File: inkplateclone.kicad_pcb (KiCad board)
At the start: 2 copper layers, 73 parts, among them J1 ED060SC7, J2 USB_C_Receptacle_USB2.0, Q1 Q_NMOS_GSD, Q2 Q_NMOS_GSD, Q3 Q_PMOS_GSD, U1 TPS65186, U2 ED097OC1, U3 MCP23017_SO, U4 ESP32-WROVER, U5 CH340C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

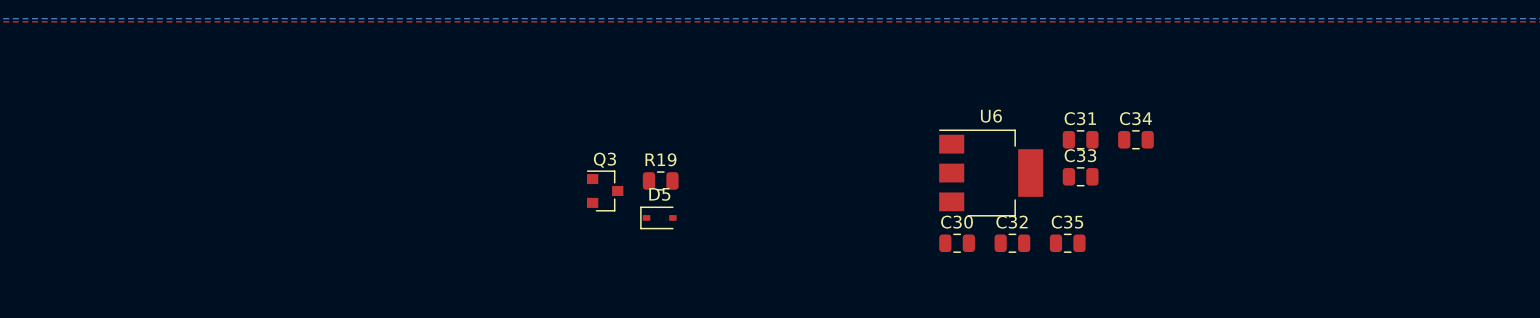
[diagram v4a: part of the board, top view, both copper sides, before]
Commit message: added charger and protection, need to verify.
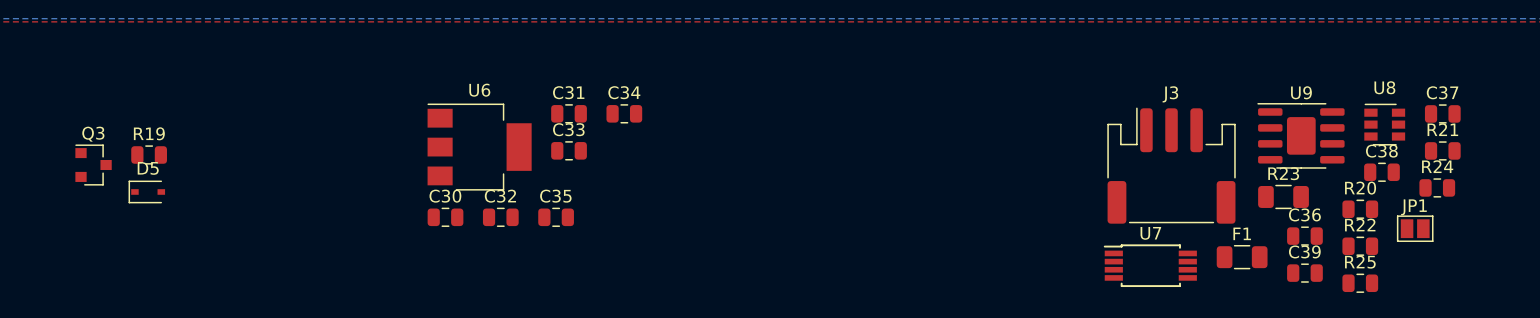
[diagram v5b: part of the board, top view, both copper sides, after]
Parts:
- added C36: 100nF, Capacitor_SMD:C_0805_2012Metric, F.Cu at (163.8, 152.2)
- added C37: 100nF, Capacitor_SMD:C_0805_2012Metric, F.Cu at (174.8, 142.5)
- added C38: 4u7, Capacitor_SMD:C_0805_2012Metric, F.Cu at (169.9, 147.1)
- added C39: 4u7, Capacitor_SMD:C_0805_2012Metric, F.Cu at (163.8, 155.2)
- added F1: Polyfuse, Fuse:Fuse_1206_3216Metric, F.Cu at (158.8, 153.9)
- added J3: Conn_01x03_Male, Connector_JST:JST_PH_S3B-PH-SM4-TB_1x03-1MP_P2.00mm_Horizontal, F.Cu at (153.2, 146.6)
- added JP1: SolderJumper_2_Open, Jumper:SolderJumper-2_P1.3mm_Open_Pad1.0x1.5mm, F.Cu at (172.6, 151.6)
- added R20: 470, Resistor_SMD:R_0805_2012Metric, F.Cu at (168.2, 150.1)
- added R21: 2K, Resistor_SMD:R_0805_2012Metric, F.Cu at (174.8, 145.4)
- added R22: 10K, Resistor_SMD:R_0805_2012Metric, F.Cu at (168.2, 153.0)
- added R23: 0R27 1/4W, Resistor_SMD:R_1206_3216Metric, F.Cu at (162.1, 149.1)
- added R24: 1.2K, Resistor_SMD:R_0805_2012Metric, F.Cu at (174.4, 148.4)
- added R25: 1.2K, Resistor_SMD:R_0805_2012Metric, F.Cu at (168.2, 156.0)
- added U7: FS8205, Package_SO:TSSOP-8_4.4x3mm_P0.65mm, F.Cu at (151.5, 154.6)
- added U8: DW-01, Package_TO_SOT_SMD:SOT-23-6, F.Cu at (170.2, 143.3)
- added U9: TP4056, Package_SO:SOIC-8-1EP_3.9x4.9mm_P1.27mm_EP2.29x3mm, F.Cu at (163.5, 144.2)
- moved C30 40.8 mm to (95.3, 150.7)
- moved C31 40.8 mm to (105.1, 142.5)
- moved C32 40.8 mm to (99.7, 150.7)
- moved C33 40.8 mm to (105.1, 145.4)
- moved C34 40.8 mm to (109.5, 142.5)
- moved C35 40.8 mm to (104.1, 150.7)
- moved D5 40.8 mm to (71.6, 148.7)
- moved Q3 40.8 mm to (67.2, 146.5)
- moved R19 40.8 mm to (71.6, 145.7)
- moved U6 40.8 mm to (98.0, 145.1)

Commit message: done some ratsnests
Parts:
- added F2: Polyfuse, Fuse:Fuse_1206_3216Metric, F.Cu at (96.3, 114.6)
- moved JP1 48.0 mm to (125.5, 160.9), turned to 90 degrees
- moved R24 44.2 mm to (131.9, 160.9), turned to 270 degrees
- moved R25 39.7 mm to (128.8, 160.9), turned to 90 degrees
- moved C37 34.3 mm to (146.1, 161.2), turned to 90 degrees
- moved U9 29.0 mm to (139.2, 160.0)
- moved R21 28.1 mm to (146.7, 146.4)
- moved Q1 26.0 mm to (114.3, 118.4)
- moved J3 25.2 mm to (161.5, 170.4)
- moved U8 25.1 mm to (146.7, 152.4)
- moved C38 24.5 mm to (149.9, 161.3), turned to 90 degrees
- moved C39 24.5 mm to (141.2, 164.6)
- moved Q2 23.5 mm to (114.3, 114.5)
- moved R23 22.4 mm to (140.2, 144.5)
- moved F1 22.3 mm to (143.6, 170.3)
- moved C35 19.8 mm to (85.7, 143.4), turned to 270 degrees
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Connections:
- J2 pad A4: +5V -> Net-(F2-Pad2)
- J2 pad A9: +5V -> Net-(F2-Pad2)
- J2 pad B4: +5V -> Net-(F2-Pad2)
- J2 pad B9: +5V -> Net-(F2-Pad2)

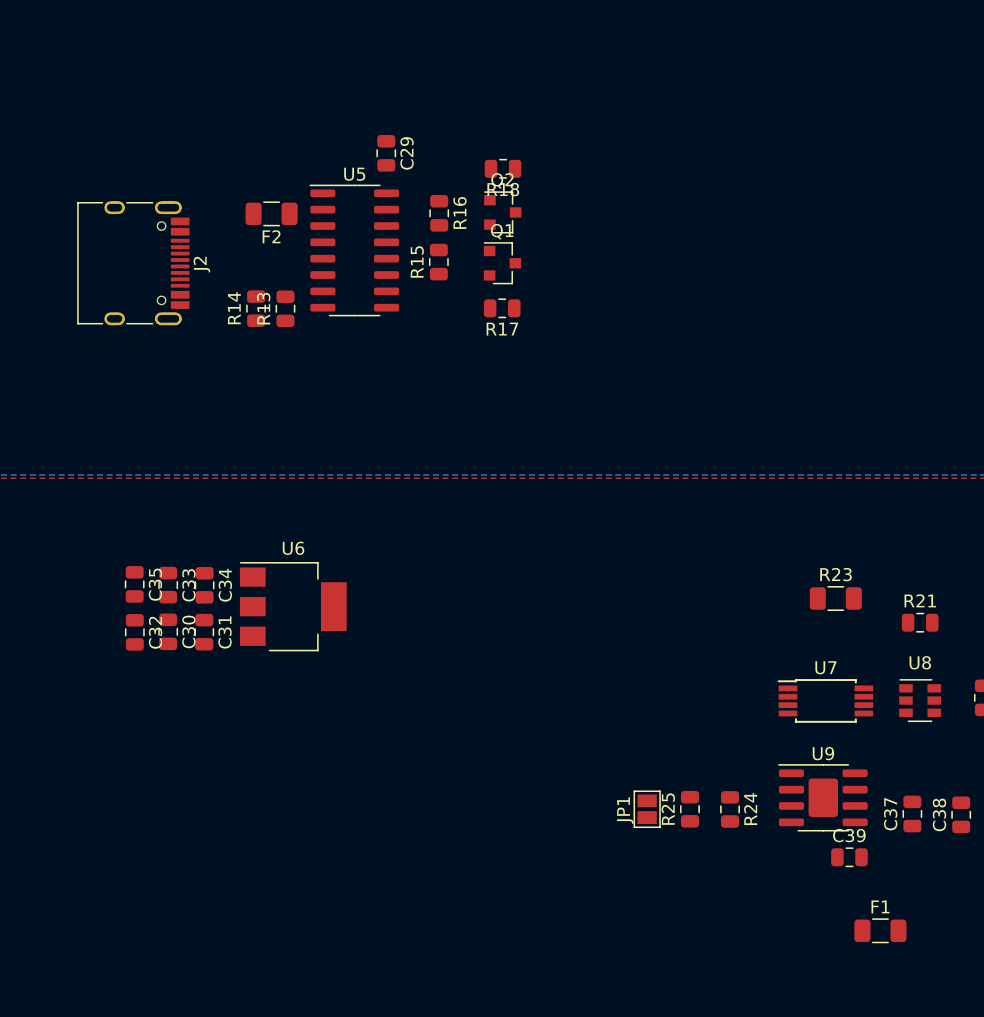
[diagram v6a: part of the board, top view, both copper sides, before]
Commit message: routed the usb c serial connection and went to town with alignment
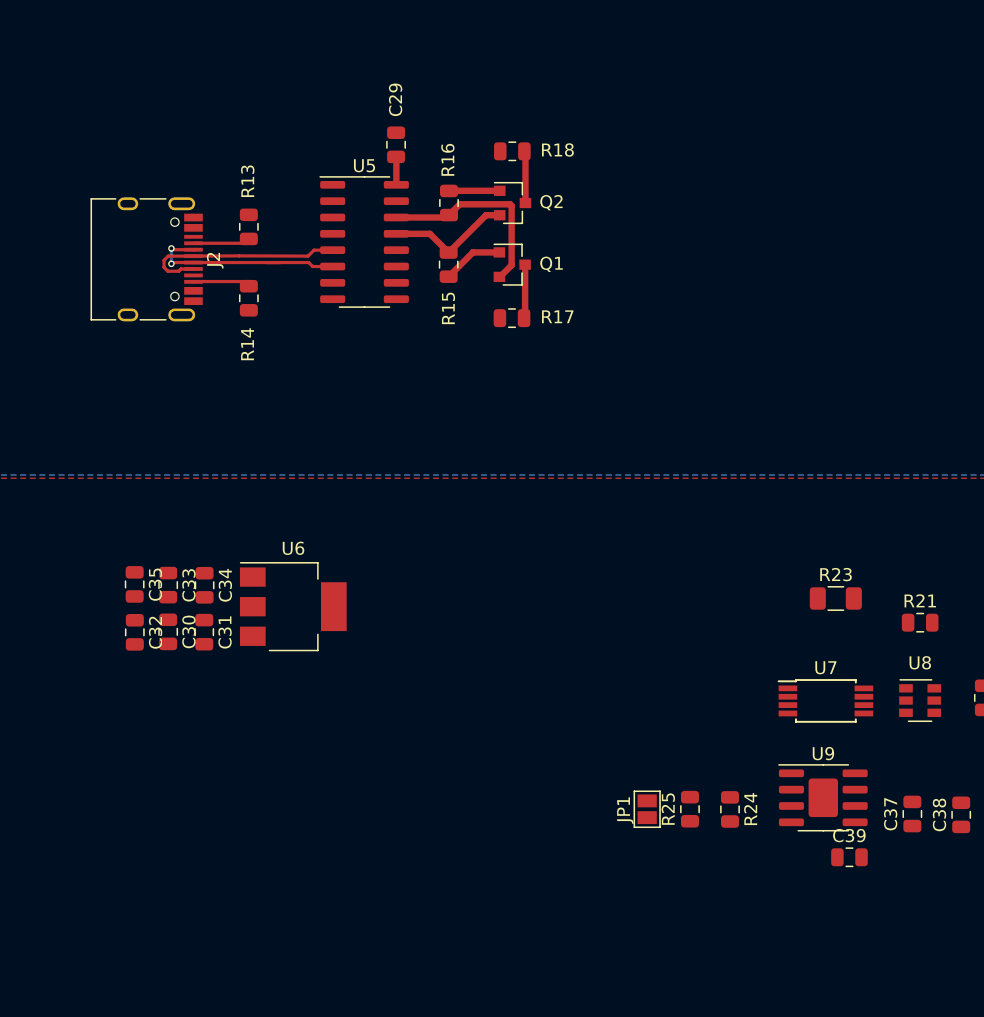
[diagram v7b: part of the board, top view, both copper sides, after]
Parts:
- removed F1, F2: Polyfuse, Fuse:Fuse_1206_3216Metric
- U6: value AMS1117-3.3 -> AP2114H-3.3TRG1
- moved R13 6.98 mm to (94.5, 115.6), turned to 270 degrees
- moved R18 1.54 mm to (115.0, 109.7)
- moved R16 1.10 mm to (110.1, 113.7)
- moved J2 1.08 mm to (86.2, 118.1)
- moved R17 1.08 mm to (115.0, 122.7)
- moved Q2 1.06 mm to (115.0, 113.7)
- moved C29 1.01 mm to (106.0, 109.2)
- moved U5 1.01 mm to (103.5, 116.8)
- moved R14 0.98 mm to (94.5, 121.1)
- moved R15 0.79 mm to (110.1, 118.5)
- moved Q1 0.77 mm to (115.0, 118.5)
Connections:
- C39 pad 2: Net-(C39-Pad2) -> VBAT
- J2 pad A4: Net-(F2-Pad2) -> +5V
- J2 pad A9: Net-(F2-Pad2) -> +5V
- J2 pad B4: Net-(F2-Pad2) -> +5V
- J2 pad B9: Net-(F2-Pad2) -> +5V
- U9 pad 5: Net-(C39-Pad2) -> VBAT
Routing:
- net /USB_DN: track 0.00 -> 16.8 mm, vias 0 -> 2
- net /USB_DP: track 0.00 -> 16.5 mm
- net SER_RTS: track 0.00 -> 15.4 mm
- net SER_DTR: track 0.00 -> 9.84 mm
- net Net-(Q1-Pad1): track 0.00 -> 4.73 mm
- net Net-(J2-PadA5): track 0.00 -> 4.44 mm
- net Net-(J2-PadB5): track 0.00 -> 4.32 mm
- net RST: track 0.00 -> 4.19 mm
- net EPD_CL: track 0.00 -> 4.05 mm
- net Net-(Q2-Pad1): track 0.00 -> 3.95 mm
- net +5V: track 0.00 -> 2.18 mm
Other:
- rule solder_mask_min_width: 0.25 -> 0.254
- rule trace_min: 0.2 -> 0.127
- rule via_min_drill: 0.3 -> 0.2
- rule via_min_size: 0.4 -> 0
